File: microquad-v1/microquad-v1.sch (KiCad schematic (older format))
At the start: 19 parts

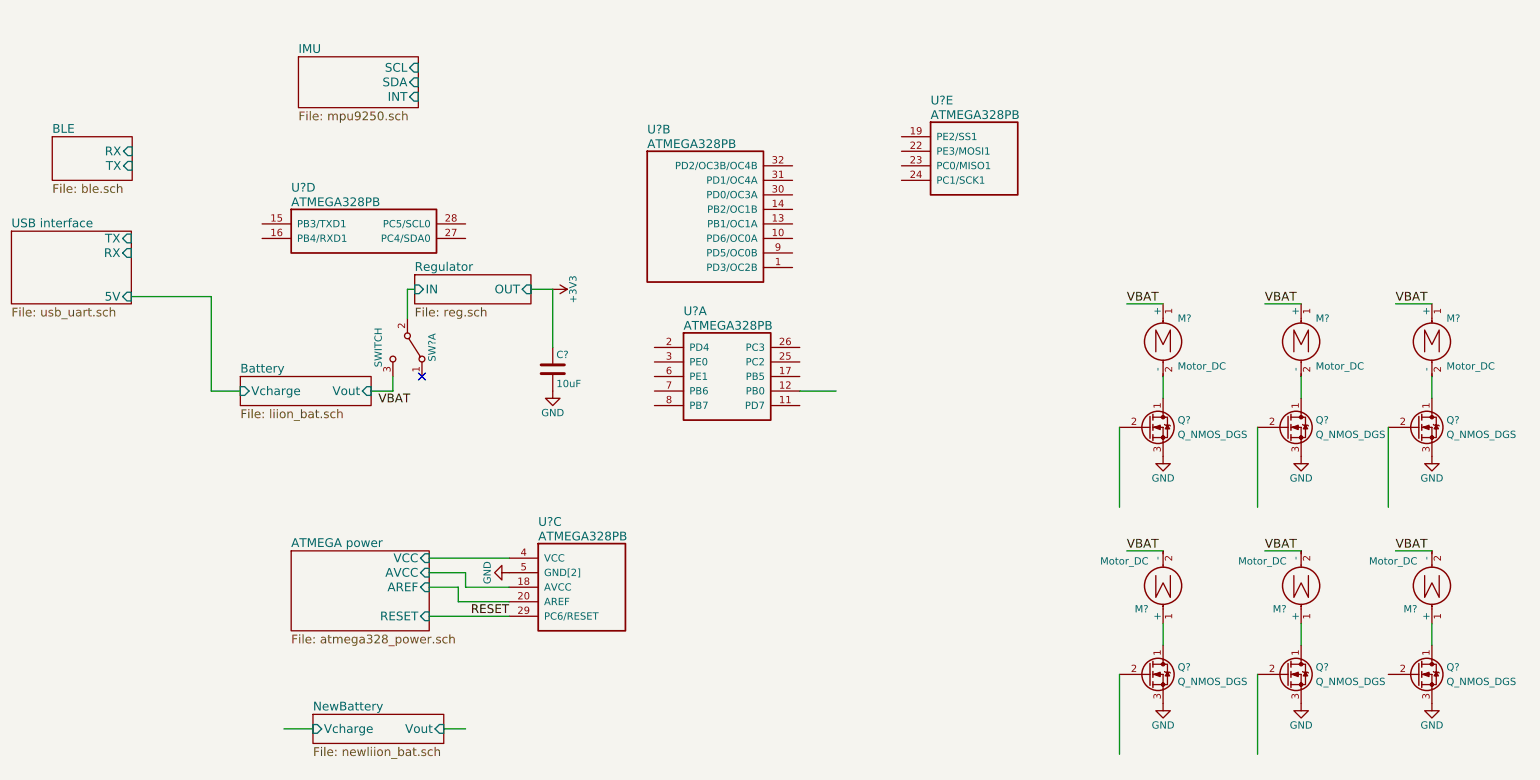
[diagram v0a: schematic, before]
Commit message: Wired in motors
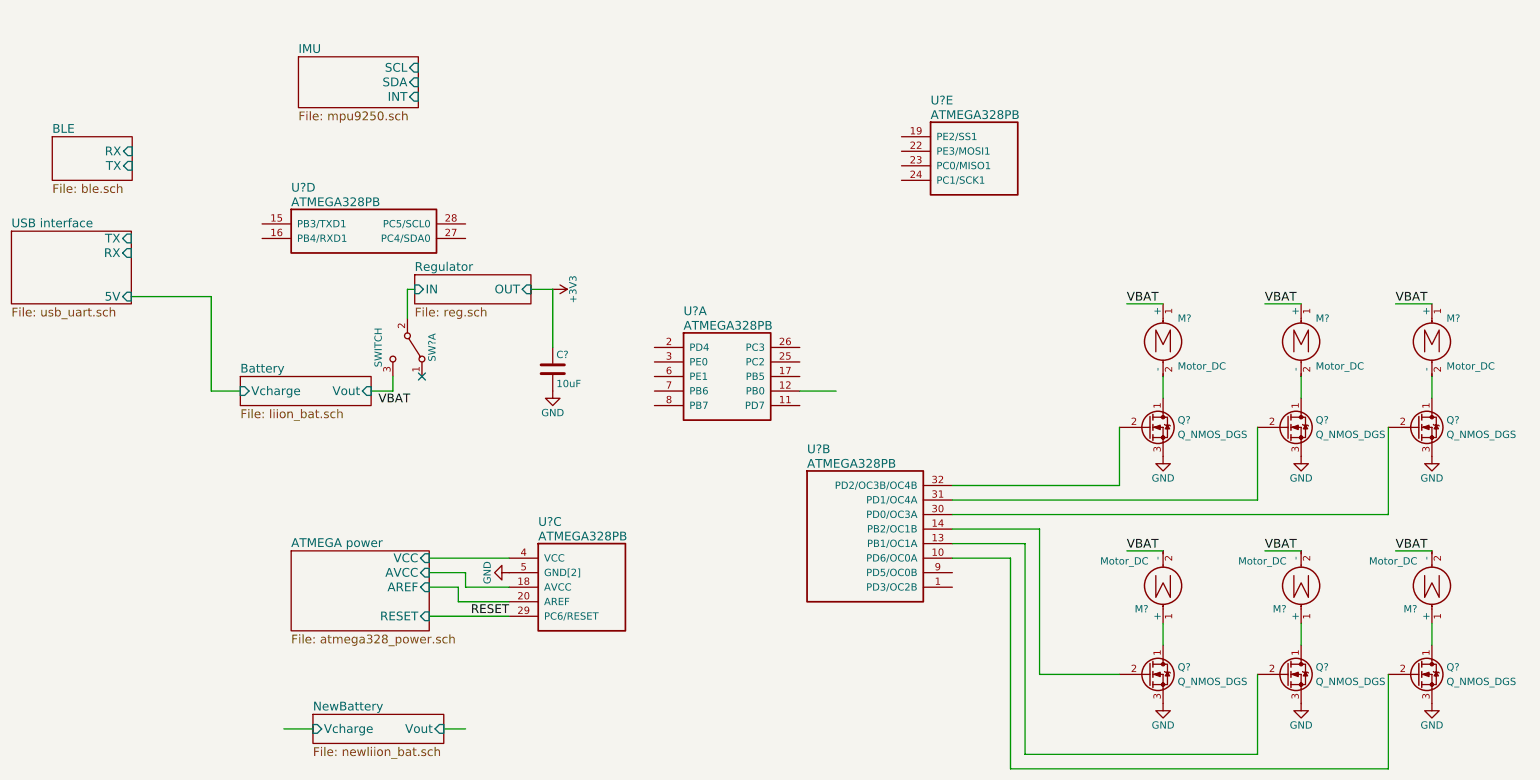
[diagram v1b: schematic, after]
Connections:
- wire segments 37 -> 49
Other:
- moved on the sheet: U?B
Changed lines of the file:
@@
 $Descr A4 11693 8268
 encoding utf-8
-Sheet 1 10
+Sheet 1 8
 Title ""
 Date ""
@@
 L ATMEGA328PB U?
 U 2 1 59F26F3B
-P 4900 1850
-F 0 "U?" H 5100 2100 60  0000 L CNN
-F 1 "ATMEGA328PB" H 5100 2000 60  0000 L CNN
-F 2 "" H 4900 1850 60  0001 C CNN
-F 3 "" H 4900 1850 60  0001 C CNN
-	2    4900 1850
+P 6000 4050
+F 0 "U?" H 6200 4300 60  0000 L CNN
+F 1 "ATMEGA328PB" H 6200 4200 60  0000 L CNN
+F 2 "" H 6000 4050 60  0001 C CNN
+F 3 "" H 6000 4050 60  0001 C CNN
+	2    6000 4050
 	1    0    0    -1
 $EndComp
@@
 Wire Wire Line
 	9600 3300 9600 3450
-Wire Wire Line
-	9300 3650 9300 4200
-Wire Wire Line
-	8350 3650 8350 4200
 $Comp
 L Q_NMOS_DGS Q?
@@
 	10500 3300 10500 3450
 Wire Wire Line
-	10200 3650 10200 4200
+	10200 3650 10200 4250
 $Comp
 L Q_NMOS_DGS Q?
@@
 Wire Wire Line
 	9300 5350 9300 5900
-Wire Wire Line
-	8350 5350 8350 5900
 $Comp
 L Q_NMOS_DGS Q?
@@
 Wire Wire Line
 	2600 5725 2800 5725
+Wire Wire Line
+	8350 3650 8350 4050
+Wire Wire Line
+	8350 4050 7200 4050
+Wire Wire Line
+	7200 4150 9300 4150
+Wire Wire Line
+	9300 4150 9300 3650
+Wire Wire Line
+	10200 4250 7200 4250
+Wire Wire Line
+	8350 5350 7800 5350
+Wire Wire Line
+	7800 5350 7800 4350
+Wire Wire Line
+	7800 4350 7200 4350
+Wire Wire Line
+	9300 5900 7700 5900
+Wire Wire Line
+	7700 5900 7700 4450
+Wire Wire Line
+	7700 4450 7200 4450
+Wire Wire Line
+	10200 5350 10200 6000
+Wire Wire Line
+	10200 6000 7600 6000
+Wire Wire Line
+	7600 6000 7600 4550
+Wire Wire Line
+	7600 4550 7200 4550
 $EndSCHEMATC

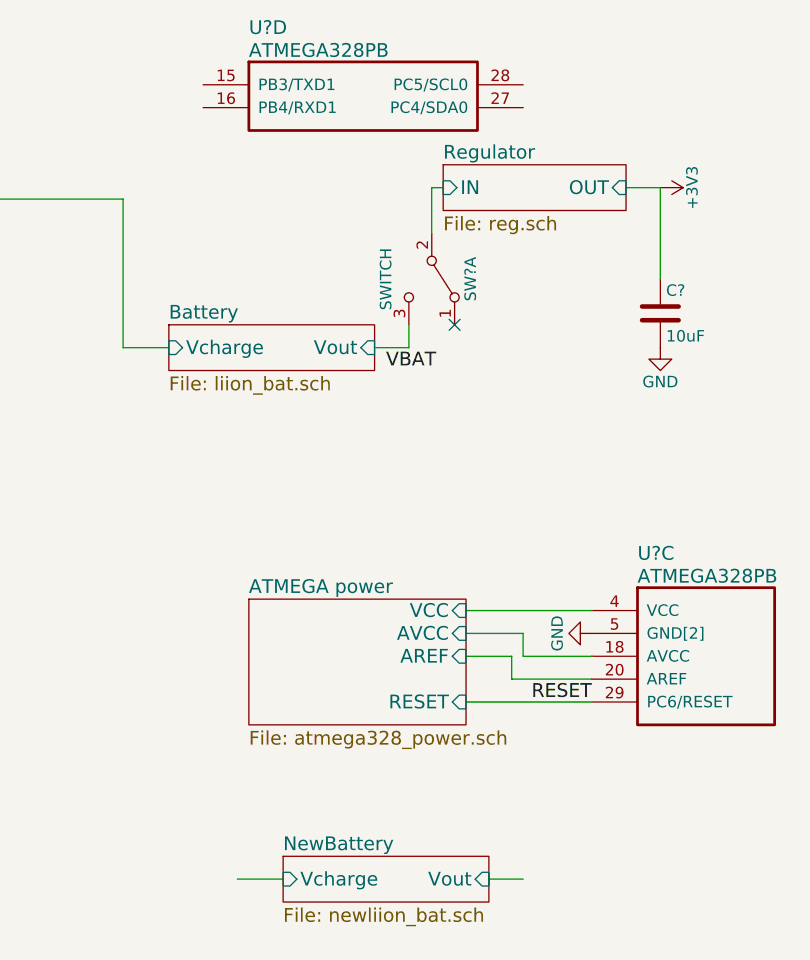
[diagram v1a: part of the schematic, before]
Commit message: Switched battery and merged some more stuff
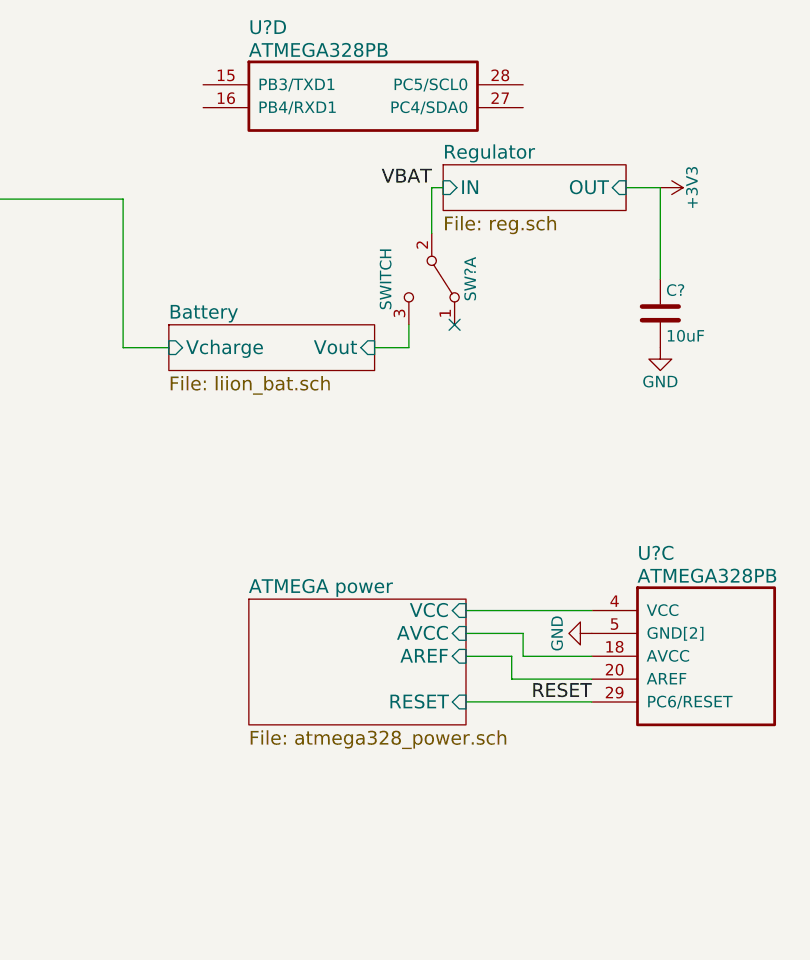
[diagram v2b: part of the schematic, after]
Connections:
- wire segments 49 -> 47
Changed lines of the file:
@@
 $Descr A4 11693 8268
 encoding utf-8
-Sheet 1 8
+Sheet 1 7
 Title ""
 Date ""
@@
 Wire Wire Line
 	2100 3400 2300 3400
-Text Label 3250 3500 0    60   ~ 0
+Text Label 3450 2700 2    60   ~ 0
 VBAT
 $Sheet
@@
 Wire Wire Line
 	6150 3400 6400 3400
-$Sheet
-S 2800 5625 900  200
-U 59F6680F
-F0 "NewBattery" 60
-F1 "newliion_bat.sch" 60
-F2 "Vout" I R 3700 5725 60
-F3 "Vcharge" I L 2800 5725 60
-$EndSheet
-Wire Wire Line
-	3700 5725 3850 5725
-Wire Wire Line
-	2600 5725 2800 5725
 Wire Wire Line
 	8350 3650 8350 4050

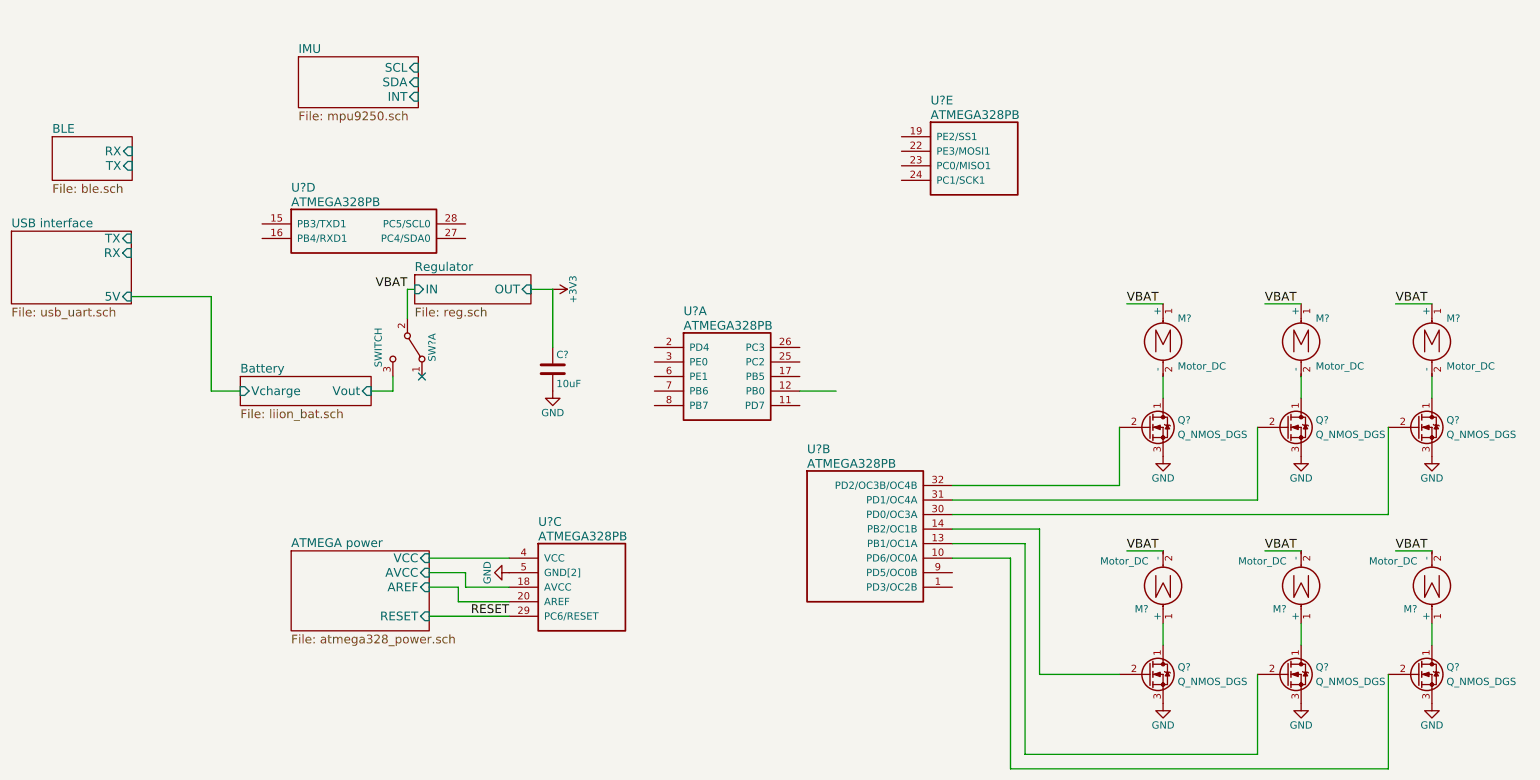
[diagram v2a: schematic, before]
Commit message: Add switch, LEDs, and no connector marks (probably still missing some, I'm not sure what all you still need
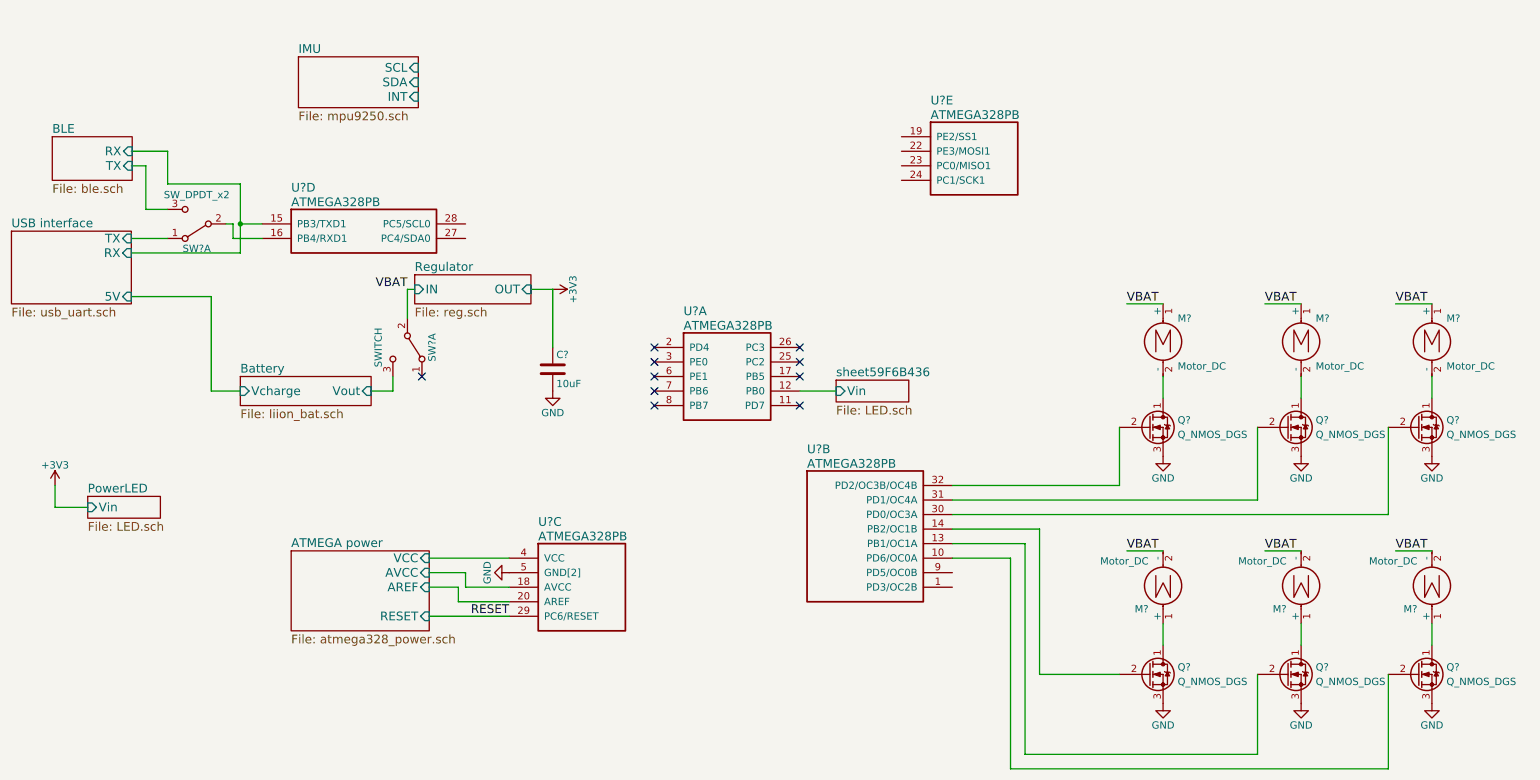
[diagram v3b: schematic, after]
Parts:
- added SW?: SW_DPDT_x2, symbol SW_DPDT_x2
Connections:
- wire segments 47 -> 62
- no-connect marks 1 -> 10
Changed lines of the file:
@@
 $Descr A4 11693 8268
 encoding utf-8
-Sheet 1 7
+Sheet 1 8
 Title ""
 Date ""
@@
 Wire Wire Line
 	7600 4550 7200 4550
+$Comp
+L SW_DPDT_x2 SW?
+U 1 1 59F6779C
+P 2000 2250
+F 0 "SW?" H 2000 2420 50  0000 C CNN
+F 1 "SW_DPDT_x2" H 2000 2050 50  0000 C CNN
+F 2 "" H 2000 2250 50  0001 C CNN
+F 3 "" H 2000 2250 50  0001 C CNN
+	1    2000 2250
+	-1   0    0    1
+$EndComp
+Wire Wire Line
+	1550 1850 1650 1850
+Wire Wire Line
+	1650 1850 1650 2150
+Wire Wire Line
+	1650 2150 1800 2150
+Wire Wire Line
+	1550 1750 1800 1750
+Wire Wire Line
+	1800 1750 1800 1975
+Wire Wire Line
+	1800 1975 2300 1975
+Wire Wire Line
+	2300 1975 2300 2450
+Wire Wire Line
+	2300 2250 2450 2250
+Wire Wire Line
+	2450 2350 2250 2350
+Wire Wire Line
+	2250 2350 2250 2250
+Wire Wire Line
+	2250 2250 2200 2250
+Wire Wire Line
+	1800 2350 1550 2350
+Wire Wire Line
+	2300 2450 1550 2450
+Connection ~ 2300 2250
+$Sheet
+S 1250 4125 500  150
+U 59F6B2DC
+F0 "PowerLED" 60
+F1 "LED.sch" 60
+F2 "Vin" I L 1250 4200 60
+$EndSheet
+$Sheet
+S 6400 3325 500  150
+U 59F6B438
+F0 "sheet59F6B436" 60
+F1 "LED.sch" 60
+F2 "Vin" I L 6400 3400 60
+$EndSheet
+$Comp
+L +3V3 #PWR?
+U 1 1 59F6B9F3
+P 1025 4050
+F 0 "#PWR?" H 1025 3900 50  0001 C CNN
+F 1 "+3V3" H 1025 4190 50  0000 C CNN
+F 2 "" H 1025 4050 50  0001 C CNN
+F 3 "" H 1025 4050 50  0001 C CNN
+	1    1025 4050
+	1    0    0    -1
+$EndComp
+Wire Wire Line
+	1025 4050 1025 4200
+Wire Wire Line
+	1025 4200 1250 4200
+NoConn ~ 6150 3100
+NoConn ~ 6150 3200
+NoConn ~ 6150 3300
+NoConn ~ 6150 3500
+NoConn ~ 5150 3500
+NoConn ~ 5150 3400
+NoConn ~ 5150 3300
+NoConn ~ 5150 3200
+NoConn ~ 5150 3100
 $EndSCHEMATC

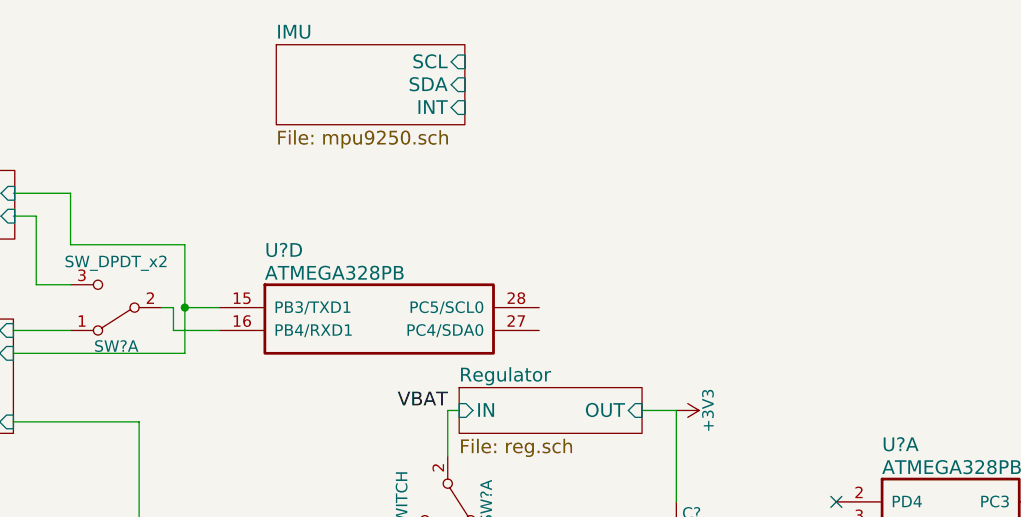
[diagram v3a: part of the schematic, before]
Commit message: Wired in IMU
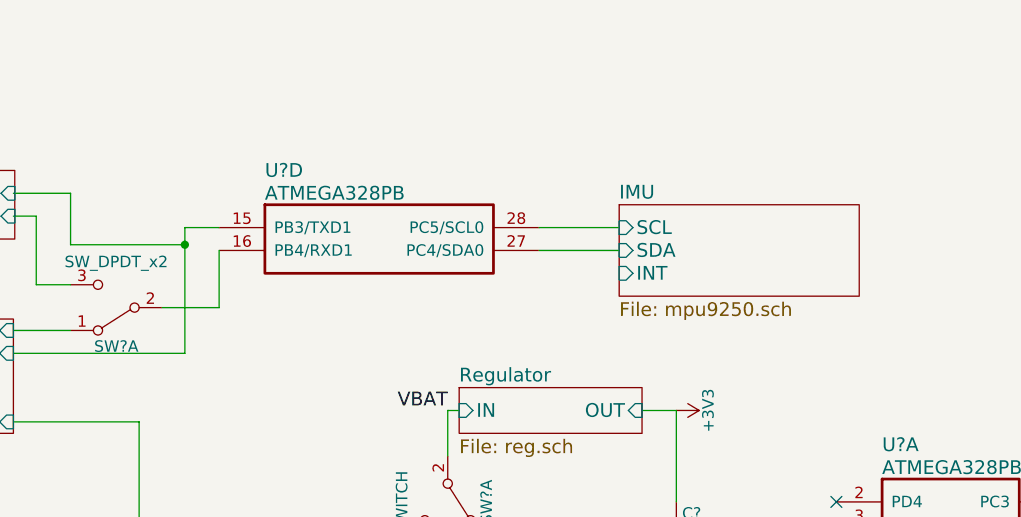
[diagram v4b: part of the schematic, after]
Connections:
- wire segments 62 -> 64
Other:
- moved on the sheet: U?D
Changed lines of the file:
@@
 L ATMEGA328PB U?
 U 4 1 59F27516
-P 2450 2250
-F 0 "U?" H 2650 2500 60  0000 L CNN
-F 1 "ATMEGA328PB" H 2650 2400 60  0000 L CNN
-F 2 "" H 2450 2250 60  0001 C CNN
-F 3 "" H 2450 2250 60  0001 C CNN
-	4    2450 2250
+P 2450 1900
+F 0 "U?" H 2650 2150 60  0000 L CNN
+F 1 "ATMEGA328PB" H 2650 2050 60  0000 L CNN
+F 2 "" H 2450 1900 60  0001 C CNN
+F 3 "" H 2450 1900 60  0001 C CNN
+	4    2450 1900
 	1    0    0    -1
 $EndComp
@@
 Text Label 3450 2700 2    60   ~ 0
 VBAT
-$Sheet
-S 2700 1100 825  350
-U 59F5A3F3
-F0 "IMU" 60
-F1 "mpu9250.sch" 60
-F2 "SCL" I R 3525 1175 60
-F3 "SDA" I R 3525 1275 60
-F4 "INT" I R 3525 1375 60
-$EndSheet
 $Comp
 L SW_DPDT_x2 SW?
@@
 	1800 1975 2300 1975
 Wire Wire Line
+	2300 1900 2300 1975
+Wire Wire Line
 	2300 1975 2300 2450
 Wire Wire Line
-	2300 2250 2450 2250
-Wire Wire Line
-	2450 2350 2250 2350
-Wire Wire Line
-	2250 2350 2250 2250
-Wire Wire Line
-	2250 2250 2200 2250
+	2300 1900 2450 1900
+Wire Wire Line
+	2450 2250 2450 2000
+Wire Wire Line
+	2200 2250 2450 2250
 Wire Wire Line
 	1800 2350 1550 2350
 Wire Wire Line
 	2300 2450 1550 2450
-Connection ~ 2300 2250
+Connection ~ 2300 1975
 $Sheet
 S 1250 4125 500  150
@@
 NoConn ~ 5150 3200
 NoConn ~ 5150 3100
+Wire Wire Line
+	3850 1900 4200 1900
+Wire Wire Line
+	4200 2000 3850 2000
+$Sheet
+S 4200 1800 1050 400
+U 59F74A78
+F0 "IMU" 60
+F1 "mpu9250.sch" 60
+F2 "SCL" I L 4200 1900 60
+F3 "SDA" I L 4200 2000 60
+F4 "INT" I L 4200 2100 60
+$EndSheet
 $EndSCHEMATC
